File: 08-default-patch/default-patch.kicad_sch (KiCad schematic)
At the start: 24 parts

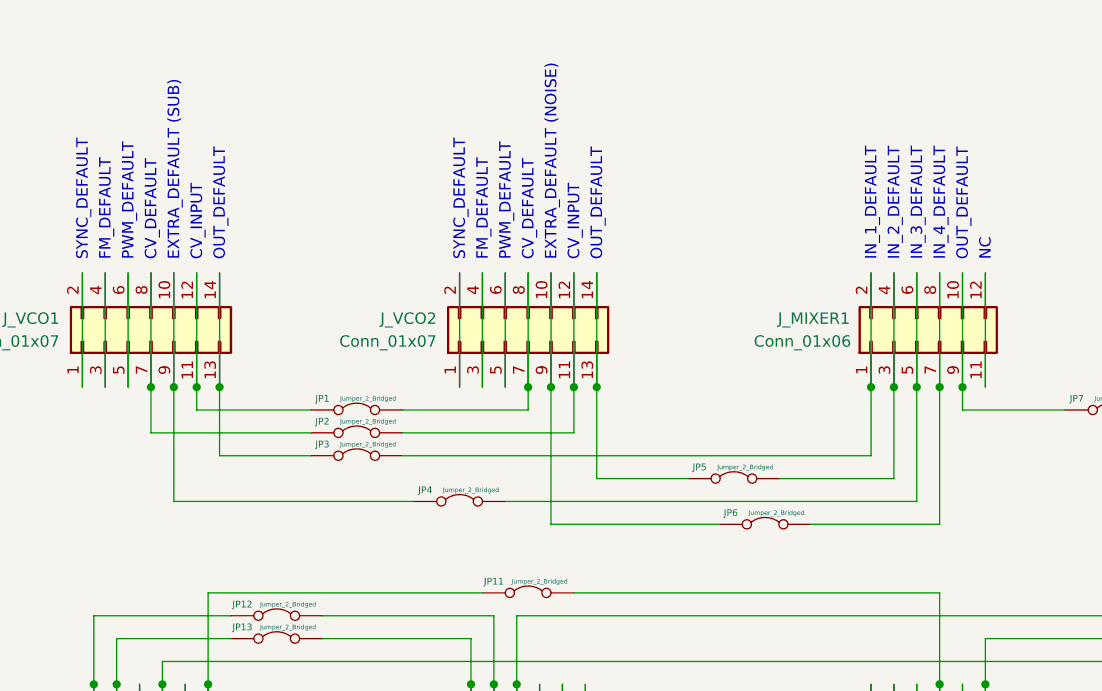
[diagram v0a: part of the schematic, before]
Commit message: Updated default patch for noise <> SUB
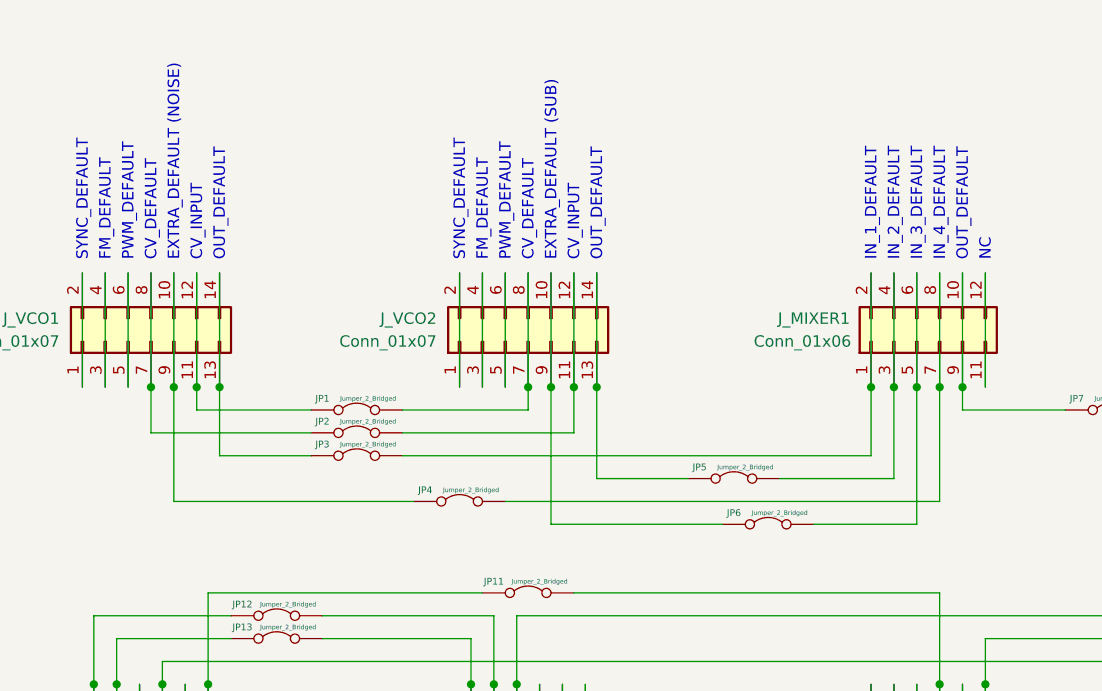
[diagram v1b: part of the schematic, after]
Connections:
- net at J_MIXER1.5 (Pin_5), J_MIXER1.6 (Pin_6): now also JP6.2 (B); no longer JP4.2 (B)
- net at J_MIXER1.7 (Pin_7), J_MIXER1.8 (Pin_8): now also JP4.2 (B); no longer JP6.2 (B)
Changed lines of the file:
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@@
 		)
 	)
-	(text "EXTRA_DEFAULT (NOISE)"
+	(text "EXTRA_DEFAULT (SUB)"
 		(exclude_from_sim no)
 		(at 121.92 63.5 90)
@@
 		)
 	)
-	(text "EXTRA_DEFAULT (SUB)"
+	(text "EXTRA_DEFAULT (NOISE)"
 		(exclude_from_sim no)
 		(at 80.01 63.5 90)
@@
 	)
 	(junction
+		(at 162.56 77.47)
+		(diameter 0)
+		(color 0 0 0 0)
+	)
+	(junction
 		(at 82.55 77.47)
 		(diameter 0)
@@
 	)
 	(junction
-		(at 162.56 77.47)
-		(diameter 0)
-		(color 0 0 0 0)
-	)
-	(junction
 		(at 165.1 110.49)
 		(diameter 0)
@@
 	)
 	(junction
+		(at 165.1 77.47)
+		(diameter 0)
+		(color 0 0 0 0)
+	)
+	(junction
 		(at 124.46 77.47)
 		(diameter 0)
@@
 	)
 	(junction
-		(at 165.1 77.47)
-		(diameter 0)
-		(color 0 0 0 0)
-	)
-	(junction
 		(at 121.92 77.47)
 		(diameter 0)
@@
 	(wire
 		(pts
-			(xy 150.7886 92.71) (xy 165.1 92.71)
-		)
-		(stroke
-			(width 0)
-			(type default)
-		)
-	)
-	(wire
-		(pts
 			(xy 83.82 100.33) (xy 114.3 100.33)
 		)
@@
 	(wire
 		(pts
-			(xy 121.92 92.71) (xy 140.6286 92.71)
+			(xy 121.92 92.71) (xy 140.97 92.71)
 		)
 		(stroke
@@
 	(wire
 		(pts
-			(xy 116.84 90.17) (xy 162.56 90.17)
+			(xy 116.84 90.17) (xy 165.1 90.17)
 		)
 		(stroke
@@
 	(wire
 		(pts
+			(xy 162.56 92.71) (xy 162.56 77.47)
+		)
+		(stroke
+			(width 0)
+			(type default)
+		)
+	)
+	(wire
+		(pts
 			(xy 205.74 105.41) (xy 205.74 91.44)
 		)
@@
 	(wire
 		(pts
-			(xy 162.56 90.17) (xy 162.56 77.47)
-		)
-		(stroke
-			(width 0)
-			(type default)
-		)
-	)
-	(wire
-		(pts
 			(xy 189.23 80.01) (xy 203.2 80.01)
 		)
@@
 	(wire
 		(pts
-			(xy 165.1 92.71) (xy 165.1 77.47)
-		)
-		(stroke
-			(width 0)
-			(type default)
-		)
-	)
-	(wire
-		(pts
 			(xy 119.38 64.77) (xy 119.38 77.47)
 		)
@@
 	(wire
 		(pts
+			(xy 151.13 92.71) (xy 162.56 92.71)
+		)
+		(stroke
+			(width 0)
+			(type default)
+		)
+	)
+	(wire
+		(pts
 			(xy 203.2 80.01) (xy 203.2 77.47)
 		)
@@
 		(pts
 			(xy 127 64.77) (xy 127 77.47)
+		)
+		(stroke
+			(width 0)
+			(type default)
+		)
+	)
+	(wire
+		(pts
+			(xy 165.1 90.17) (xy 165.1 77.47)
 		)
 		(stroke
@@
 	(symbol
 		(lib_id "Jumper:Jumper_2_Bridged")
-		(at 145.7086 92.71 0)
+		(at 146.05 92.71 0)
 		(unit 1)
 		(exclude_from_sim no)
@@
 		(dnp no)
 		(property "Reference" "JP6"
-			(at 141.8986 91.44 0)
+			(at 142.24 91.44 0)
 			(effects
 				(font
@@
 		)
 		(property "Value" "Jumper_2_Bridged"
-			(at 146.9786 91.44 0)
+			(at 147.32 91.44 0)
 			(effects
 				(font
@@
 		)
 		(property "Footprint" "Jumper:SolderJumper-2_P1.3mm_Bridged_RoundedPad1.0x1.5mm"
-			(at 145.7086 92.71 0)
+			(at 146.05 92.71 0)
 			(effects
 				(font
@@
 		)
 		(property "Datasheet" "~"
-			(at 145.7086 92.71 0)
+			(at 146.05 92.71 0)
 			(effects
 				(font
@@
 		)
 		(property "Description" "Jumper, 2-pole, closed/bridged"
-			(at 145.7086 92.71 0)
+			(at 146.05 92.71 0)
 			(effects
 				(font
@@
 		)
 		(property "Part No." ""
-			(at 145.7086 92.71 0)
+			(at 146.05 92.71 0)
 			(effects
 				(font
@@
 		)
 		(property "Part URL" ""
-			(at 145.7086 92.71 0)
+			(at 146.05 92.71 0)
 			(effects
 				(font
@@
 		)
 		(property "Vendor" ""
-			(at 145.7086 92.71 0)
+			(at 146.05 92.71 0)
 			(effects
 				(font
@@
 		)
 		(property "LCSC" ""
-			(at 145.7086 92.71 0)
-			(effects
-				(font
+			(at 146.05 92.71 0)
+			(effects
+				(font

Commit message: Reverted default patch
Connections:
- net at J_MIXER1.7 (Pin_7), J_MIXER1.8 (Pin_8): now also JP6.2 (B); no longer JP4.2 (B)
- net at J_MIXER1.5 (Pin_5), J_MIXER1.6 (Pin_6): now also JP4.2 (B); no longer JP6.2 (B)
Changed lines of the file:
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@@
 		)
 	)
-	(text "EXTRA_DEFAULT (SUB)"
+	(text "EXTRA_DEFAULT (NOISE)"
 		(exclude_from_sim no)
 		(at 121.92 63.5 90)
@@
 		)
 	)
-	(text "EXTRA_DEFAULT (NOISE)"
+	(text "EXTRA_DEFAULT (SUB)"
 		(exclude_from_sim no)
 		(at 80.01 63.5 90)
@@
 	)
 	(junction
+		(at 82.55 77.47)
+		(diameter 0)
+		(color 0 0 0 0)
+	)
+	(junction
+		(at 170.18 110.49)
+		(diameter 0)
+		(color 0 0 0 0)
+	)
+	(junction
+		(at 78.74 110.49)
+		(diameter 0)
+		(color 0 0 0 0)
+	)
+	(junction
+		(at 77.47 77.47)
+		(diameter 0)
+		(color 0 0 0 0)
+	)
+	(junction
+		(at 115.57 110.49)
+		(diameter 0)
+		(color 0 0 0 0)
+	)
+	(junction
+		(at 85.09 77.47)
+		(diameter 0)
+		(color 0 0 0 0)
+	)
+	(junction
+		(at 80.01 77.47)
+		(diameter 0)
+		(color 0 0 0 0)
+	)
+	(junction
+		(at 157.48 77.47)
+		(diameter 0)
+		(color 0 0 0 0)
+	)
+	(junction
+		(at 205.74 77.47)
+		(diameter 0)
+		(color 0 0 0 0)
+	)
+	(junction
+		(at 73.66 110.49)
+		(diameter 0)
+		(color 0 0 0 0)
+	)
+	(junction
 		(at 162.56 77.47)
 		(diameter 0)
@@
 	)
 	(junction
-		(at 82.55 77.47)
-		(diameter 0)
-		(color 0 0 0 0)
-	)
-	(junction
-		(at 170.18 110.49)
-		(diameter 0)
-		(color 0 0 0 0)
-	)
-	(junction
-		(at 78.74 110.49)
-		(diameter 0)
-		(color 0 0 0 0)
-	)
-	(junction
-		(at 77.47 77.47)
-		(diameter 0)
-		(color 0 0 0 0)
-	)
-	(junction
-		(at 115.57 110.49)
-		(diameter 0)
-		(color 0 0 0 0)
-	)
-	(junction
-		(at 85.09 77.47)
-		(diameter 0)
-		(color 0 0 0 0)
-	)
-	(junction
-		(at 80.01 77.47)
-		(diameter 0)
-		(color 0 0 0 0)
-	)
-	(junction
-		(at 157.48 77.47)
-		(diameter 0)
-		(color 0 0 0 0)
-	)
-	(junction
-		(at 205.74 77.47)
-		(diameter 0)
-		(color 0 0 0 0)
-	)
-	(junction
-		(at 73.66 110.49)
-		(diameter 0)
-		(color 0 0 0 0)
-	)
-	(junction
 		(at 165.1 110.49)
 		(diameter 0)
@@
 	)
 	(junction
+		(at 124.46 77.47)
+		(diameter 0)
+		(color 0 0 0 0)
+	)
+	(junction
+		(at 210.82 77.47)
+		(diameter 0)
+		(color 0 0 0 0)
+	)
+	(junction
+		(at 83.82 110.49)
+		(diameter 0)
+		(color 0 0 0 0)
+	)
+	(junction
+		(at 119.38 77.47)
+		(diameter 0)
+		(color 0 0 0 0)
+	)
+	(junction
 		(at 165.1 77.47)
 		(diameter 0)
@@
 	)
 	(junction
-		(at 124.46 77.47)
-		(diameter 0)
-		(color 0 0 0 0)
-	)
-	(junction
-		(at 210.82 77.47)
-		(diameter 0)
-		(color 0 0 0 0)
-	)
-	(junction
-		(at 83.82 110.49)
-		(diameter 0)
-		(color 0 0 0 0)
-	)
-	(junction
-		(at 119.38 77.47)
-		(diameter 0)
-		(color 0 0 0 0)
-	)
-	(junction
 		(at 121.92 77.47)
 		(diameter 0)
@@
 	(wire
 		(pts
+			(xy 150.7886 92.71) (xy 165.1 92.71)
+		)
+		(stroke
+			(width 0)
+			(type default)
+		)
+	)
+	(wire
+		(pts
 			(xy 83.82 100.33) (xy 114.3 100.33)
 		)
@@
 	(wire
 		(pts
-			(xy 121.92 92.71) (xy 140.97 92.71)
+			(xy 121.92 92.71) (xy 140.6286 92.71)
 		)
 		(stroke
@@
 	(wire
 		(pts
-			(xy 116.84 90.17) (xy 165.1 90.17)
+			(xy 116.84 90.17) (xy 162.56 90.17)
 		)
 		(stroke
@@
 	(wire
 		(pts
-			(xy 162.56 92.71) (xy 162.56 77.47)
-		)
-		(stroke
-			(width 0)
-			(type default)
-		)
-	)
-	(wire
-		(pts
 			(xy 205.74 105.41) (xy 205.74 91.44)
 		)
@@
 	(wire
 		(pts
+			(xy 162.56 90.17) (xy 162.56 77.47)
+		)
+		(stroke
+			(width 0)
+			(type default)
+		)
+	)
+	(wire
+		(pts
 			(xy 189.23 80.01) (xy 203.2 80.01)
 		)
@@
 	(wire
 		(pts
+			(xy 165.1 92.71) (xy 165.1 77.47)
+		)
+		(stroke
+			(width 0)
+			(type default)
+		)
+	)
+	(wire
+		(pts
 			(xy 119.38 64.77) (xy 119.38 77.47)
 		)
@@
 	(wire
 		(pts
-			(xy 151.13 92.71) (xy 162.56 92.71)
-		)
-		(stroke
-			(width 0)
-			(type default)
-		)
-	)
-	(wire
-		(pts
 			(xy 203.2 80.01) (xy 203.2 77.47)
 		)
@@
 		(pts
 			(xy 127 64.77) (xy 127 77.47)
-		)
-		(stroke
-			(width 0)
-			(type default)
-		)
-	)
-	(wire
-		(pts
-			(xy 165.1 90.17) (xy 165.1 77.47)
 		)
 		(stroke
@@
 	(symbol
 		(lib_id "Jumper:Jumper_2_Bridged")
-		(at 146.05 92.71 0)
+		(at 145.7086 92.71 0)
 		(unit 1)
 		(exclude_from_sim no)
@@
 		(dnp no)
 		(property "Reference" "JP6"
-			(at 142.24 91.44 0)
+			(at 141.8986 91.44 0)
 			(effects
 				(font
@@
 		)
 		(property "Value" "Jumper_2_Bridged"
-			(at 147.32 91.44 0)
+			(at 146.9786 91.44 0)
 			(effects
 				(font
@@
 		)
 		(property "Footprint" "Jumper:SolderJumper-2_P1.3mm_Bridged_RoundedPad1.0x1.5mm"
-			(at 146.05 92.71 0)
+			(at 145.7086 92.71 0)
 			(effects
 				(font
@@
 		)
 		(property "Datasheet" "~"
-			(at 146.05 92.71 0)
+			(at 145.7086 92.71 0)
 			(effects
 				(font
@@
 		)
 		(property "Description" "Jumper, 2-pole, closed/bridged"
-			(at 146.05 92.71 0)
+			(at 145.7086 92.71 0)
 			(effects
 				(font
@@
 		)
 		(property "Part No." ""
-			(at 146.05 92.71 0)
+			(at 145.7086 92.71 0)
 			(effects
 				(font
@@
 		)
 		(property "Part URL" ""
-			(at 146.05 92.71 0)
+			(at 145.7086 92.71 0)
 			(effects
 				(font
@@
 		)
 		(property "Vendor" ""
-			(at 146.05 92.71 0)
+			(at 145.7086 92.71 0)
 			(effects
 				(font
@@
 		)
 		(property "LCSC" ""
-			(at 146.05 92.71 0)
-			(effects
-				(font
+			(at 145.7086 92.71 0)
+			(effects
+				(font
